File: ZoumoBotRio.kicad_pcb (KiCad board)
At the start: 2 copper layers, 83.2 x 52.1 mm, 138 parts, among them CON1 BARREL_JACK, J1 Screw_Terminal_1x05, J2 Screw_Terminal_1x05, P1 USB_OTG, P10 Analog, P11 Digital, P12 Analog, P13 Digital, P14 CONN_01X06, P2 Analog, P3 Digital, P4 Analog, P5 Digital, P6 Analog, P7 Digital, P8 Analog, P9 Digital, Q1 Q_PMOS_GDS, Q2 IR Receiver, Q3 IR Receiver, U1 ZLDO1117K50TC, U2 ATmega32U4-AU, U3 SOT361-1_2, U4 TB6612FNG, U5 TB6612FNG, Y1 16MHz

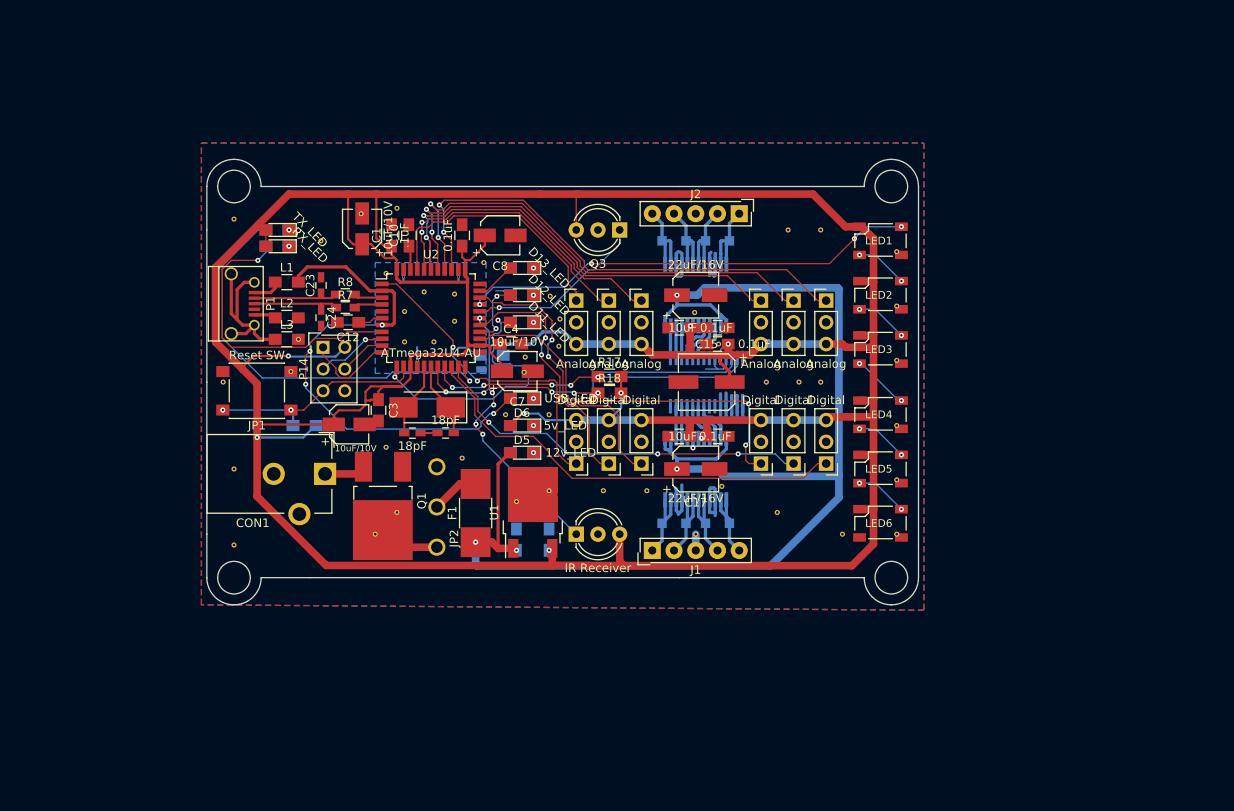
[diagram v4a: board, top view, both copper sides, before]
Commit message: Revised layout for EMI
various issues.
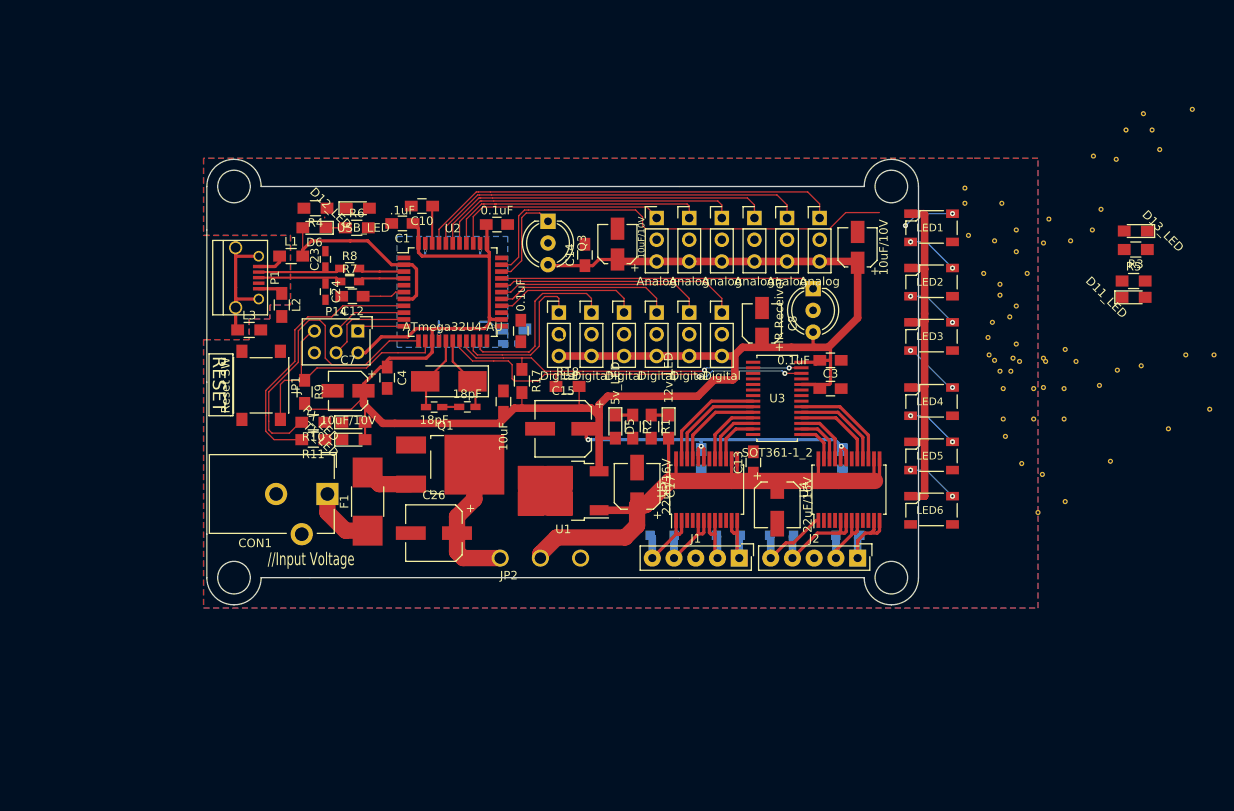
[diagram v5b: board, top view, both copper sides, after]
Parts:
- removed the REF** at (145.3, 107.6)
- removed the REF** at (145.4, 104.4)
- removed the REF** at (144.3, 101.7)
- removed the REF** at (164.0, 107.3)
- removed the REF** at (122.2, 92.1)
- removed the REF** at (141.2, 110.6)
- removed the REF** at (114.0, 110.5)
- added C26: C, Capacitors_SMD:CP_Elec_6.3x7.7, F.Cu at (130.7, 129.4)
- added REF**: VIA-.6mm, VIA:VIA-.6mm, F.Cu at (218.6, 108.6)
- added REF**: VIA-.6mm, VIA:VIA-.6mm, F.Cu at (216.5, 117.2)
- added REF**: VIA-.6mm, VIA:VIA-.6mm, F.Cu at (210.6, 110.4)
- added REF**: VIA-.6mm, VIA:VIA-.6mm, F.Cu at (213.4, 109.9)
- added REF**: VIA-.6mm, VIA:VIA-.6mm, F.Cu at (201.9, 95.5)
- added REF**: VIA-.6mm, VIA:VIA-.6mm, F.Cu at (221.4, 114.9)
- added REF**: VIA-.6mm, VIA:VIA-.6mm, F.Cu at (207.6, 94.0)
- added REF**: VIA-.6mm, VIA:VIA-.6mm, F.Cu at (224.8, 81.9)
- added REF**: VIA-.6mm, VIA:VIA-.6mm, F.Cu at (222.8, 83.9)
- added REF**: VIA-.6mm, VIA:VIA-.6mm, F.Cu at (231.5, 84.5)
- added REF**: VIA-.6mm, VIA:VIA-.6mm, F.Cu at (145.7, 106.6)
- added REF**: VIA-.6mm, VIA:VIA-.6mm, F.Cu at (222.8, 86.7)
- added REF**: VIA-.6mm, VIA:VIA-.6mm, F.Cu at (202.6, 92.7)
- added REF**: VIA-.6mm, VIA:VIA-.6mm, F.Cu at (205.1, 95.2)
- added REF**: VIA-.6mm, VIA:VIA-.6mm, F.Cu at (197.1, 90.9)
- added REF**: VIA-.6mm, VIA:VIA-.6mm, F.Cu at (227.7, 89.5)
- added REF**: VIA-.6mm, VIA:VIA-.6mm, F.Cu at (221.9, 108.6)
- C13, C14, R1, R10, R11, R2, R3, R4, R5, R6, R9, U3, U4, U5: moved to F.Cu
- C19, C22: moved to B.Cu
- moved REF** 99.8 mm to (204.3, 116.1)
- moved REF** 94.8 mm to (201.8, 122.6)
- moved REF** 92.0 mm to (198.4, 109.0)
- moved REF** 89.2 mm to (192.8, 90.9)
- moved REF** 88.7 mm to (221.4, 82.5)
- moved REF** 79.9 mm to (192.8, 89.1)
- moved REF** 78.7 mm to (196.2, 95.2)
- moved REF** 78.4 mm to (198.0, 104.1)
- moved REF** 75.0 mm to (198.8, 107.3)
- moved REF** 73.7 mm to (198.8, 96.5)
- moved REF** 73.3 mm to (198.8, 102.9)
- moved REF** 72.2 mm to (197.2, 116.1)
- moved D2 71.9 mm to (212.7, 94.1)
- moved R3 71.8 mm to (212.7, 96.3)
- moved R5 71.7 mm to (212.5, 99.9), turned to 0 degrees
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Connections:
- F1 pad 1: +12V -> Net-(CON1-Pad1)
- JP2 pad 2: Net-(F1-Pad2) -> +12V
- Q1 pad 3: Net-(CON1-Pad1) -> Net-(F1-Pad2)
- U2 pad 1: D7 -> Net-(U2-Pad1)
- U2 pad 12: D11 -> Net-(R10-Pad2)
- U2 pad 22: Net-(R11-Pad2) -> Net-(U2-Pad22)
- U2 pad 25: D4 -> Net-(U2-Pad25)
- U2 pad 26: D12 -> D4
- U2 pad 27: D6 -> D5
- U2 pad 28: D8 -> D6
- U2 pad 29: D9 -> D7
- U2 pad 30: D10 -> D8
- U2 pad 31: D5 -> D9
- U2 pad 32: D13 -> D10
- U2 pad 36: A0 -> A5
- U2 pad 37: A1 -> A4
- U2 pad 38: A2 -> A3
- U2 pad 39: A3 -> A2
- U2 pad 40: A4 -> A1
- U2 pad 41: A5 -> A0
- U2 pad 8: Net-(R10-Pad2) -> Net-(R11-Pad2)
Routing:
- net +5V: track 476.2 -> 314.5 mm, vias 9 -> 3
- net +12V: track 156.9 -> 70.6 mm, vias 4 -> 0
- net GND: track 55.1 -> 1.99 mm, vias 1 -> 0
- net UVcc: track 61.1 -> 23.9 mm, vias 4 -> 0
- net D0/RXI: track 51.8 -> 19.0 mm
- net D11: track 32.4 -> 0.00 mm, vias 2 -> 0
- net D4: track 46.7 -> 17.1 mm, vias 2 -> 0
- net D1/TXO: track 45.6 -> 21.9 mm, vias 3 -> 0
- net Net-(R11-Pad2): track 48.7 -> 31.8 mm, vias 1 -> 0
- net A2: track 52.0 -> 40.6 mm, vias 2 -> 0
- net A1: track 56.4 -> 45.4 mm, vias 2 -> 0
- net D5: track 34.1 -> 23.4 mm, vias 2 -> 0
- net D7: track 37.6 -> 28.4 mm, vias 2 -> 0
- net D9: track 21.2 -> 12.3 mm, vias 1 -> 0
- net A0: track 58.8 -> 50.2 mm, vias 2 -> 0
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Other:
- board text added: "//Input Voltage"
- board text added: "RESET"
